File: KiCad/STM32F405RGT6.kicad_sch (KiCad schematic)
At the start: 55 parts, among them J1 Conn_02x05_Odd_Even, J2 USB_C_Receptacle_USB2.0, Q1 AO3401A, SW1 TS-1187A, SW2 TS-1187A, U1 M24C02-RMN, U2 AMS1117-3.3, U3 STM32F405RGTx, Y1 16MHz

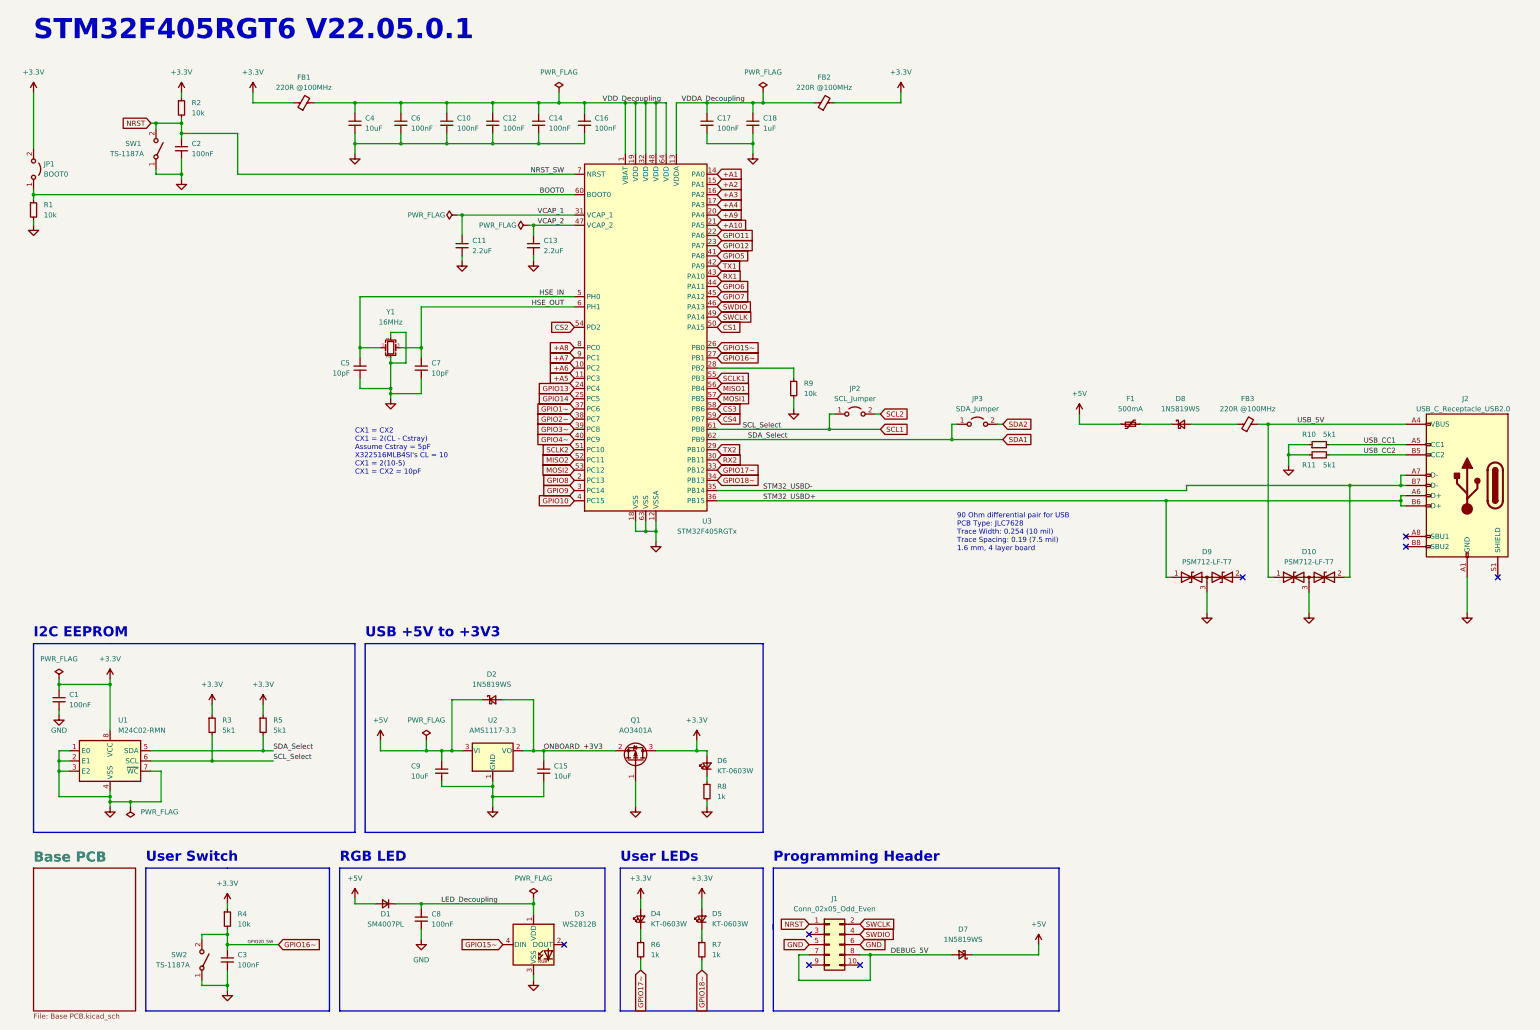
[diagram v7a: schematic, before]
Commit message: Added Datasheets
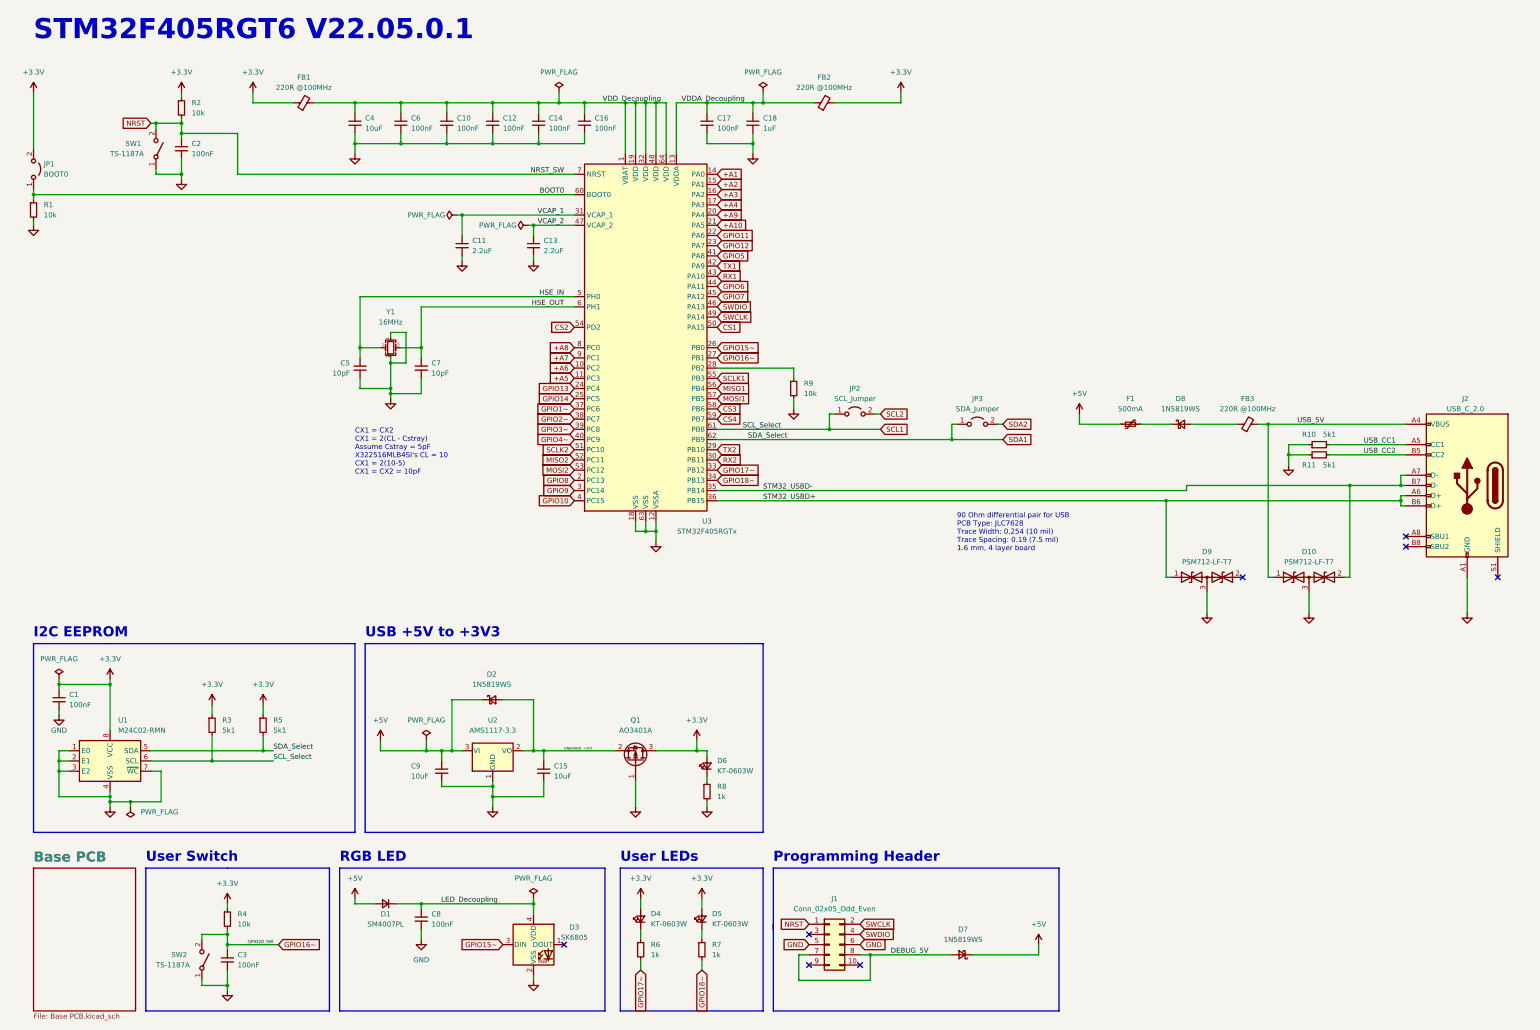
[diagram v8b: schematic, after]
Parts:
- removed D3: WS2812B, LED_SMD:LED_WS2812B_PLCC4_5.0x5.0mm_P3.2mm, symbol LED:WS2812B
- added D3: SK6805, LED_SMD:LED_SK6805_PLCC4_2.4x2.7mm_P1.3mm, symbol LED:SK6805
- J2: value USB_C_Receptacle_USB2.0 -> USB_C_2.0
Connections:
- net GND: now also D3.2 (VSS)
- net GPIO15~: now also D3.3 (DIN)
- net LED_Decoupling: now also D3.4 (VDD)
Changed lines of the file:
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@@
     (effects (font (size 1.27 1.27)) (justify right bottom))
   )
-  (label "ONBOARD_+3V3" (at 152.4 201.93 0)
-    (effects (font (size 1.27 1.27)) (justify left bottom))
+  (label "ONBOARD_+3V3" (at 157.48 201.93 0)
+    (effects (font (size 0.6 0.6)) (justify left bottom))
   )
   (label "USB_CC2" (at 364.49 128.27 180)
@@
     (pin "1")
   )
-  (symbol (lib_id "LED:WS2812B") (at 149.86 250.19 0) (unit 1)
+  (symbol (lib_id "Device:R_Small") (at 62.23 41.91 0) (unit 1)
+    (in_bom yes) (on_board yes) (fields_autoplaced)
+    (property "Reference" "R2" (id 0) (at 64.77 40.6399 0)
+      (effects (font (size 1.27 1.27)) (justify left))
+    )
+    (property "Value" "10k" (id 1) (at 64.77 43.1799 0)
+      (effects (font (size 1.27 1.27)) (justify left))
+    )
+    (property "Footprint" "Resistor_SMD:R_0603_1608Metric" (id 2) (at 62.23 41.91 0)
+      (effects (font (size 1.27 1.27)) hide)
+    )
+    (property "Datasheet" "https://datasheet.lcsc.com/lcsc/2206010045_UNI-ROYAL-Uniroyal-Elec-0603WAF1002T5E_C25804.pdf" (id 3) (at 62.23 41.91 0)
+      (effects (font (size 1.27 1.27)) hide)
+    )
+    (property "JLCPCB Part #" "C25804" (id 4) (at 62.23 41.91 0)
+      (effects (font (size 1.27 1.27)) hide)
+    )
+    (property "Part Number" "0603WAF1002T5E" (id 5) (at 62.23 41.91 0)
+      (effects (font (size 1.27 1.27)) hide)
+    )
+    (pin "1")
+    (pin "2")
+  )
+  (symbol (lib_id "LED:SK6805") (at 149.86 250.19 0) (unit 1)
     (in_bom yes) (on_board yes)
-    (property "Reference" "D3" (id 0) (at 161.29 242.57 0))
-    (property "Value" "WS2812B" (id 1) (at 161.29 245.11 0))
-    (property "Footprint" "LED_SMD:LED_WS2812B_PLCC4_5.0x5.0mm_P3.2mm" (id 2) (at 151.13 257.81 0)
+    (property "Reference" "D3" (id 0) (at 160.02 245.8593 0))
+    (property "Value" "SK6805" (id 1) (at 160.02 248.3993 0))
+    (property "Footprint" "LED_SMD:LED_SK6805_PLCC4_2.4x2.7mm_P1.3mm" (id 2) (at 151.13 257.81 0)
       (effects (font (size 1.27 1.27)) (justify left top) hide)
     )
-    (property "Datasheet" "https://cdn-shop.adafruit.com/datasheets/WS2812B.pdf" (id 3) (at 152.4 259.715 0)
+    (property "Datasheet" "https://cdn-shop.adafruit.com/product-files/3484/3484_Datasheet.pdf" (id 3) (at 152.4 259.715 0)
       (effects (font (size 1.27 1.27)) (justify left top) hide)
     )
-    (property "Mouser Part Number" "" (id 4) (at 149.86 250.19 0)
-      (effects (font (size 1.27 1.27)) hide)
-    )
-    (property "Part Number" "WS2812B-B/W" (id 5) (at 149.86 250.19 0)
-      (effects (font (size 1.27 1.27)) hide)
-    )
-    (property "JLCPCB Part #" "C2761795" (id 6) (at 149.86 250.19 0)
+    (property "JLCPCB Part #" "C2890035" (id 4) (at 149.86 250.19 0)
       (effects (font (size 1.27 1.27)) hide)
     )
@@
     (pin "3")
     (pin "4")
-  )
-  (symbol (lib_id "Device:R_Small") (at 62.23 41.91 0) (unit 1)
-    (in_bom yes) (on_board yes) (fields_autoplaced)
-    (property "Reference" "R2" (id 0) (at 64.77 40.6399 0)
-      (effects (font (size 1.27 1.27)) (justify left))
-    )
-    (property "Value" "10k" (id 1) (at 64.77 43.1799 0)
-      (effects (font (size 1.27 1.27)) (justify left))
-    )
-    (property "Footprint" "Resistor_SMD:R_0603_1608Metric" (id 2) (at 62.23 41.91 0)
-      (effects (font (size 1.27 1.27)) hide)
-    )
-    (property "Datasheet" "https://datasheet.lcsc.com/lcsc/2206010045_UNI-ROYAL-Uniroyal-Elec-0603WAF1002T5E_C25804.pdf" (id 3) (at 62.23 41.91 0)
-      (effects (font (size 1.27 1.27)) hide)
-    )
-    (property "JLCPCB Part #" "C25804" (id 4) (at 62.23 41.91 0)
-      (effects (font (size 1.27 1.27)) hide)
-    )
-    (property "Part Number" "0603WAF1002T5E" (id 5) (at 62.23 41.91 0)
-      (effects (font (size 1.27 1.27)) hide)
-    )
-    (pin "1")
-    (pin "2")
   )
   (symbol (lib_id "power:+3.3V") (at 191.77 238.76 0) (unit 1)
@@
       (effects (font (size 1.27 1.27)) (justify right))
     )
-    (property "Value" "USB_C_Receptacle_USB2.0" (id 1) (at 369.57 116.84 0)
+    (property "Value" "USB_C_2.0" (id 1) (at 377.19 116.84 0)
       (effects (font (size 1.27 1.27)) (justify right))
     )
@@
       (reference "D2") (unit 1) (value "1N5819WS") (footprint "Diode_SMD:D_SOD-323")
     )
-    (path "/3c8ac9aa-3104-4098-858a-84849faa6053"
-      (reference "D3") (unit 1) (value "WS2812B") (footprint "LED_SMD:LED_WS2812B_PLCC4_5.0x5.0mm_P3.2mm")
+    (path "/3ed6005b-ffdb-4ba0-b625-cd66834bbdef"
+      (reference "D3") (unit 1) (value "SK6805") (footprint "LED_SMD:LED_SK6805_PLCC4_2.4x2.7mm_P1.3mm")
     )
     (path "/b1a11706-8ba7-4dfe-bb8a-754c60587f7c"
@@
     )
     (path "/bff70746-9e66-4d49-9e56-80db00d0272e"
-      (reference "J2") (unit 1) (value "USB_C_Receptacle_USB2.0") (footprint "Connector_USB:USB_C_Receptacle_HRO_TYPE-C-31-M-12")
+      (reference "J2") (unit 1) (value "USB_C_2.0") (footprint "Connector_USB:USB_C_Receptacle_HRO_TYPE-C-31-M-12")
     )
     (path "/00000000-0000-0000-0000-000061aa1a42/00000000-0000-0000-0000-000061b06a26"
